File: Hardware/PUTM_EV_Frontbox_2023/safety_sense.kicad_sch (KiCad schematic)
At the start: 2 parts, among them U6 TLP291-4, U7 TLP291-4

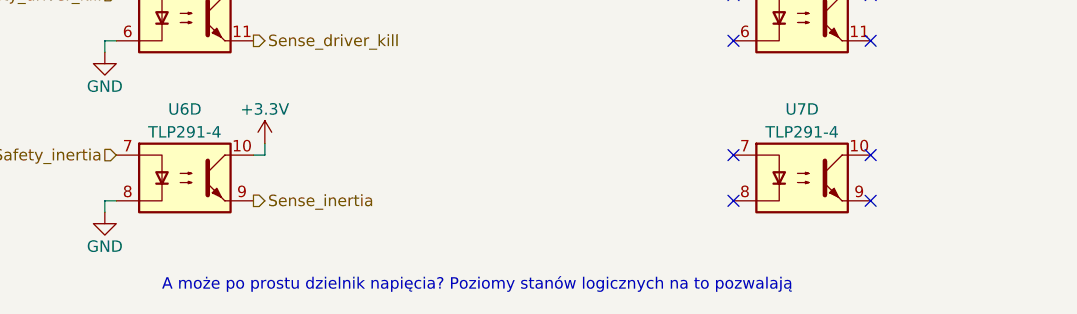
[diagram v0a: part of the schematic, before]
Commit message: Added power section, replaced SWPS
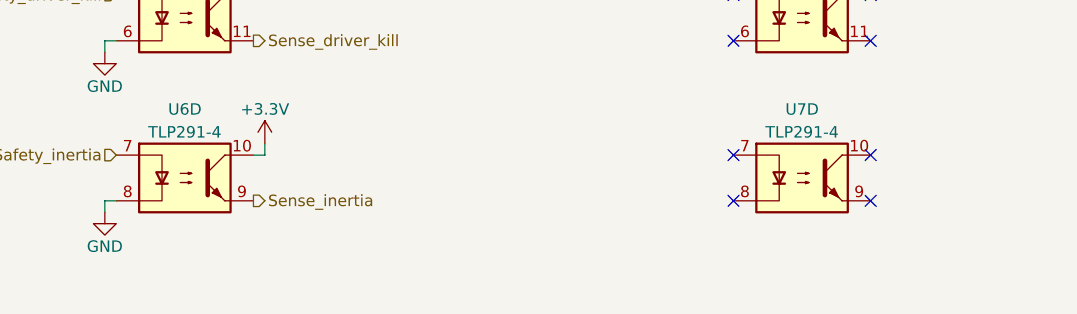
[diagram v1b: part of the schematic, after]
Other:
- note removed: "A może po prostu dzielnik napięcia? Poziomy stanów logicznych na to pozwalają"
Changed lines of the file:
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@@
     (stroke (width 0) (type default))
-  )
-  (text "A może po prostu dzielnik napięcia? Poziomy stanów logicznych na to pozwalają"
-    (at 110.49 142.24 0)
-    (effects (font (size 1.27 1.27)) (justify left bottom))
   )
   (hierarchical_label "Safety_right_kill" (shape input) (at 105.41 92.71 180) (fields_autoplaced)

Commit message: Schematic ready for review
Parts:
- removed unit 4 of U7
- added R11, R12, R13, R14, R15, R16: 5k, symbol Device:R_Small
- renumbered U6 to U10, U7 to U11
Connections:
- net Safety_BSPD: now also R15.1; no longer U11.1
- net Safety_driver_kill: now also R13.1; no longer U10.5
- net Safety_inertia: now also R14.1; no longer U10.7
- net Safety_left_kill: now also R11.1; no longer U10.1
- net Safety_overtravel: now also R16.1; no longer U11.3
- net Safety_right_kill: now also R12.1; no longer U10.3
- new net: R16.2, U11.3
- new net: R12.2, U10.3
- new net: R11.2, U10.1
- new net: R14.2, U10.7
- new net: R13.2, U10.5
- new net: R15.2, U11.1
- no-connect marks 8 -> 4
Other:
- note added: "The remaining optocoupler is used to translate laptimer states"
- moved on the sheet: U10B, U10C, U10D, U11B, U11C

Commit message: Fixed all issues
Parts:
- added R79, R80, R81, R82, R83, R84: 10k, symbol Device:R_Small
- R11, R12, R13, R14, R15, R16: value 5k -> 2k
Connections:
- net +3.3V: now also R79.1, R80.1, R81.1, R82.1, R83.1, R84.1; no longer U10.10, U10.12, U10.14, U10.16, U11.14, U11.16
- net GND: now also U10.11, U10.13, U10.15, U10.9, U11.13, U11.15
- net Sense_BSPD: now also U11.16, R83.2; no longer U11.15
- net Sense_driver_kill: now also U10.12, R81.2; no longer U10.11
- net Sense_inertia: now also U10.10, R82.2; no longer U10.9
- net Sense_left_kill: now also U10.16, R79.2; no longer U10.15
- net Sense_overtravel: now also U11.14, R84.2; no longer U11.13
- net Sense_right_kill: now also U10.14, R80.2; no longer U10.13
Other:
- moved on the sheet: R12, R13, R14, R16, U10B, U10C, U10D, U11B, U11C

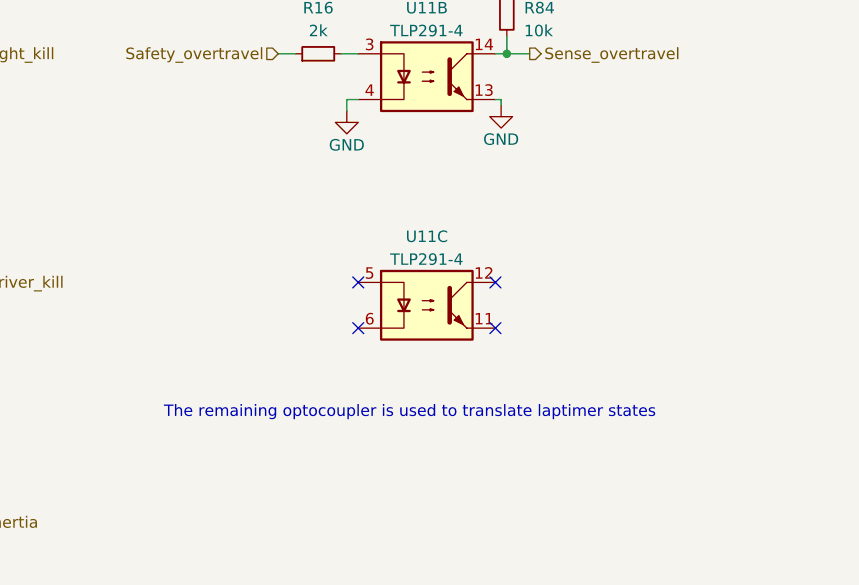
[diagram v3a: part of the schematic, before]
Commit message: Schematic modified, footprints assigned
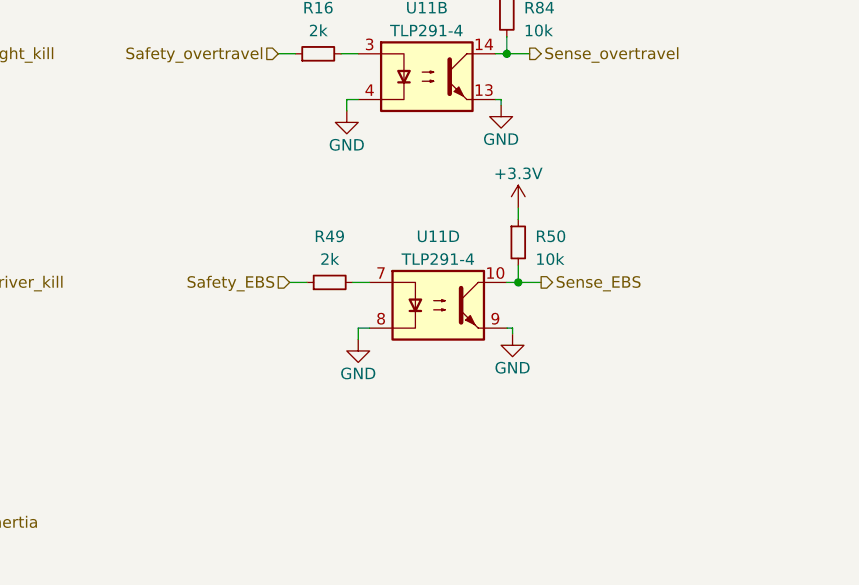
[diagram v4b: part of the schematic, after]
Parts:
- removed unit 3 of U11
- added R49: 2k, Resistor_SMD:R_0402_1005Metric, symbol Device:R_Small
- added R50: 10k, Resistor_SMD:R_0402_1005Metric, symbol Device:R_Small
- added unit 4 of U11
- R11, R12, R13, R14, R15, R16, R79, R80, R81, R82, R83, R84: footprint (none) -> Resistor_SMD:R_0402_1005Metric
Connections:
- net +3.3V: now also R50.1
- net GND: now also U11.8, U11.9
- new net: R49.2, U11.7
- new net Safety_EBS: R49.1
- new net Sense_EBS: R50.2, U11.10
- no-connect marks 4 -> 0
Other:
- note removed: "The remaining optocoupler is used to translate laptimer states"

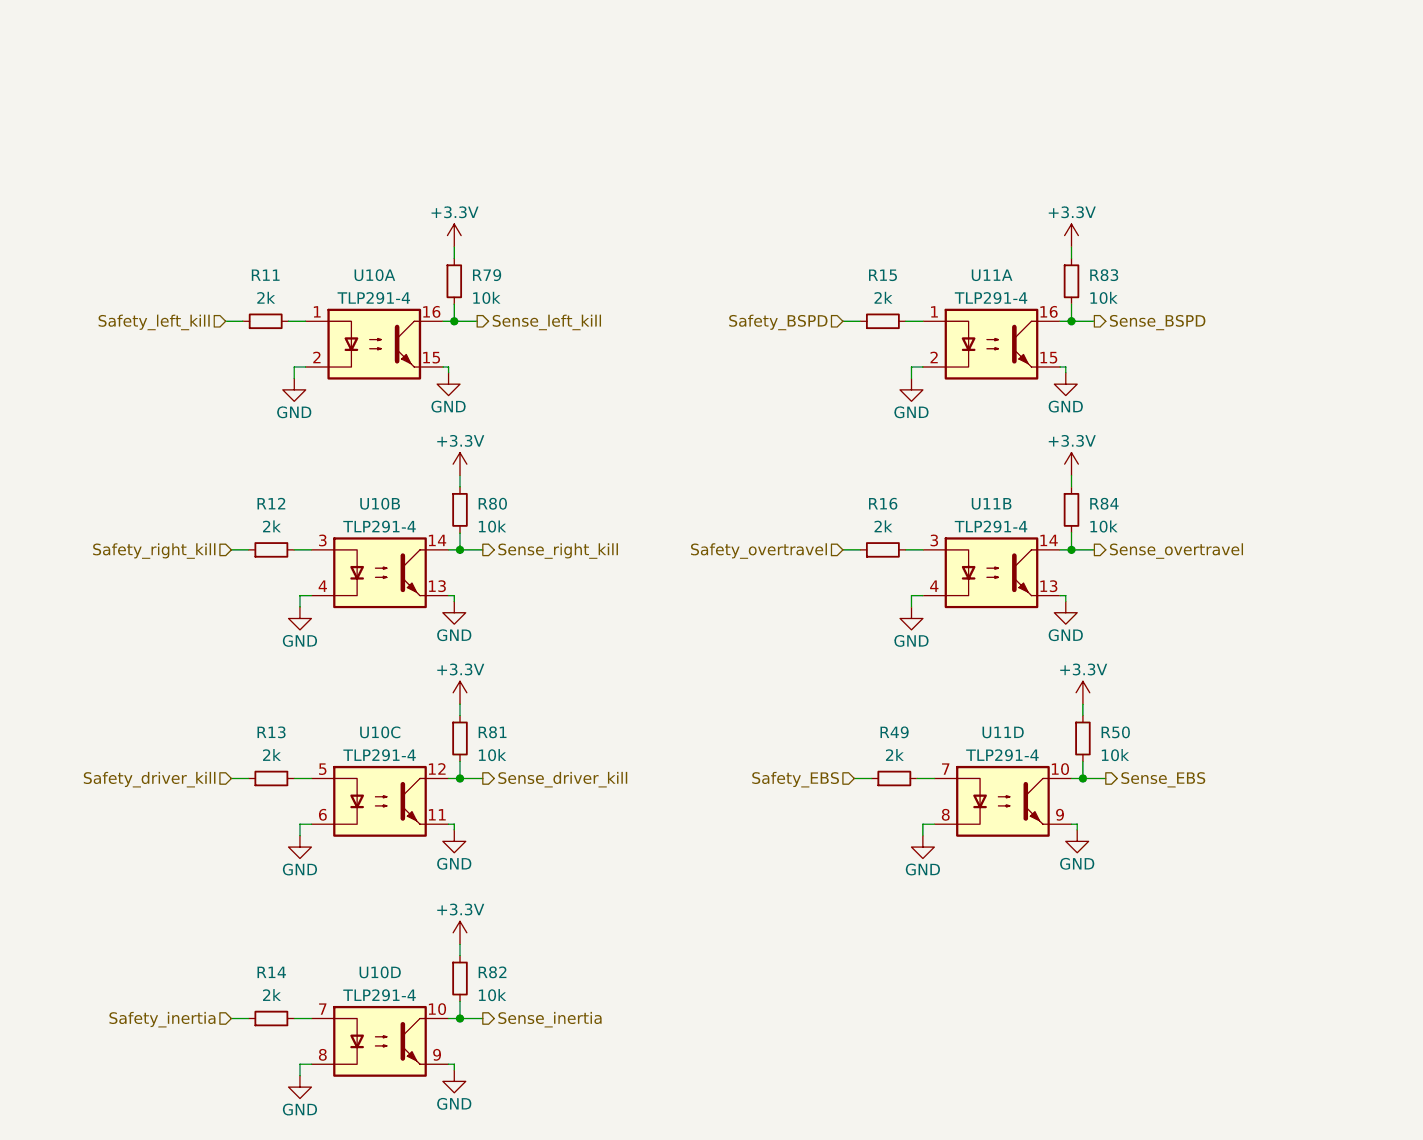
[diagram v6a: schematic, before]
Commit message: Changed board outline and layout to match ASB
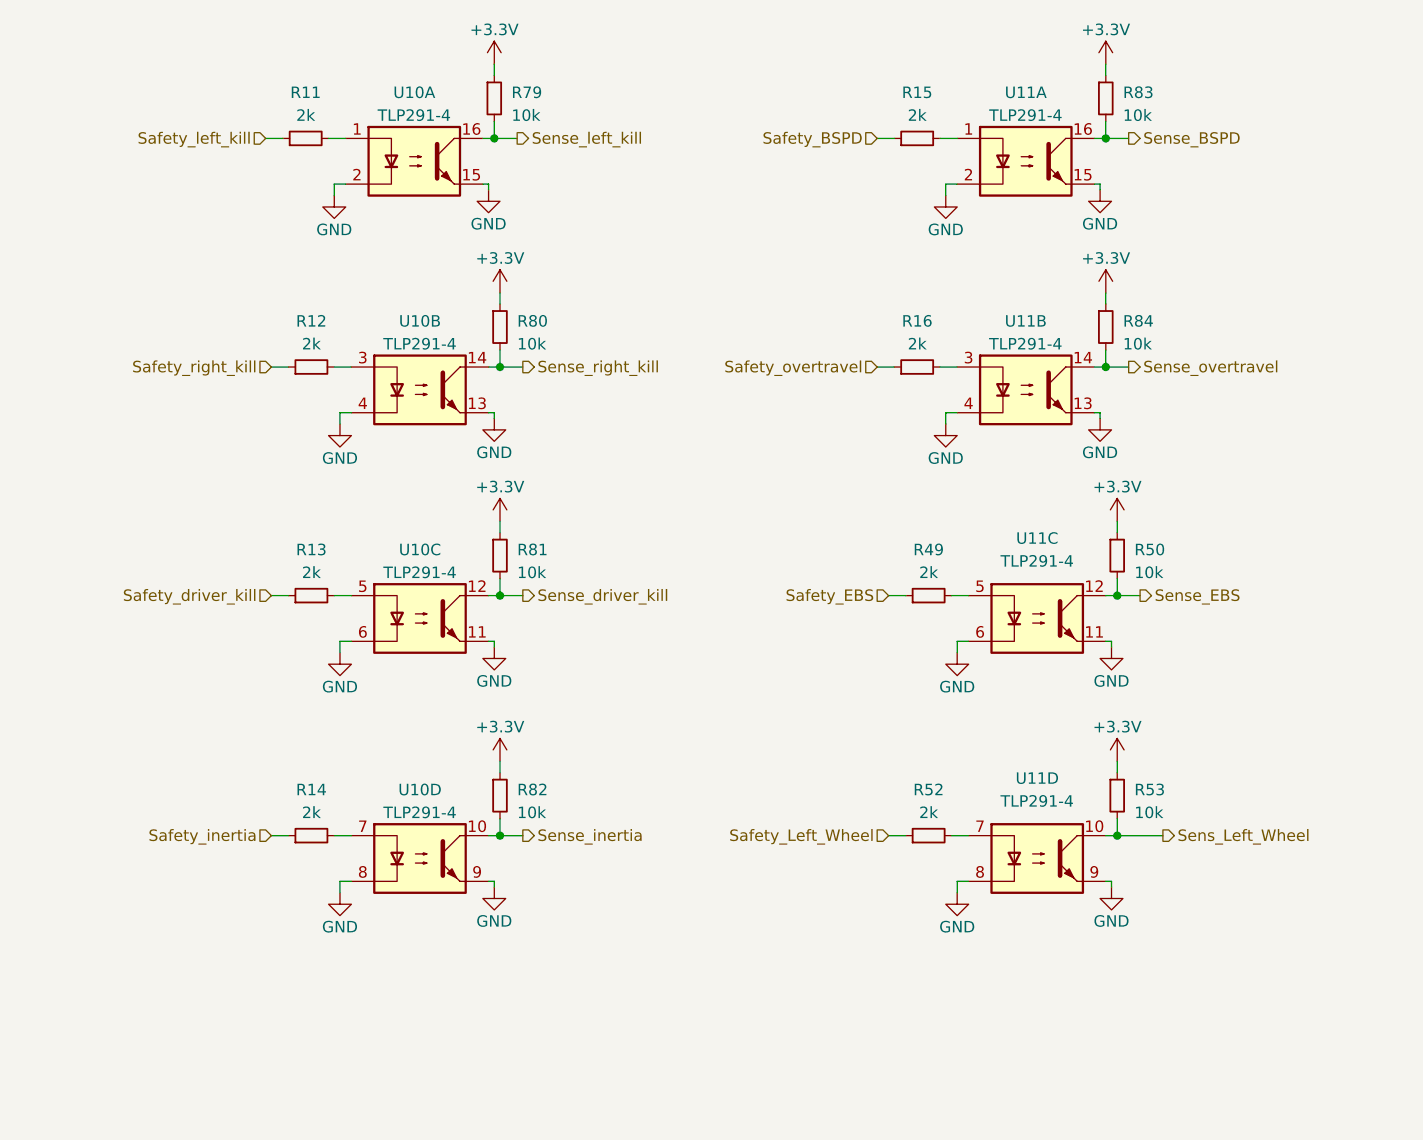
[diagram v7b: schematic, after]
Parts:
- added R52: 2k, Resistor_SMD:R_0402_1005Metric, symbol Device:R_Small
- added R53: 10k, Resistor_SMD:R_0402_1005Metric, symbol Device:R_Small
- added unit 4 of U11
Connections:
- net +3.3V: now also R53.1
- net GND: now also U11.11, U11.6, U11.8, U11.9; no longer U11.8, U11.9
- net Sense_EBS: now also U11.12; no longer U11.10
- net at R49.2: now also U11.5; no longer U11.7
- new net: R52.2, U11.7
- new net Safety_Left_Wheel: R52.1
- new net Sens_Left_Wheel: R53.2, U11.10
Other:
- moved on the sheet: R11, R12, R13, R14, R15, R16, R49, R50, R79, R80, R81, R82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

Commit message: Changed mcu pinout
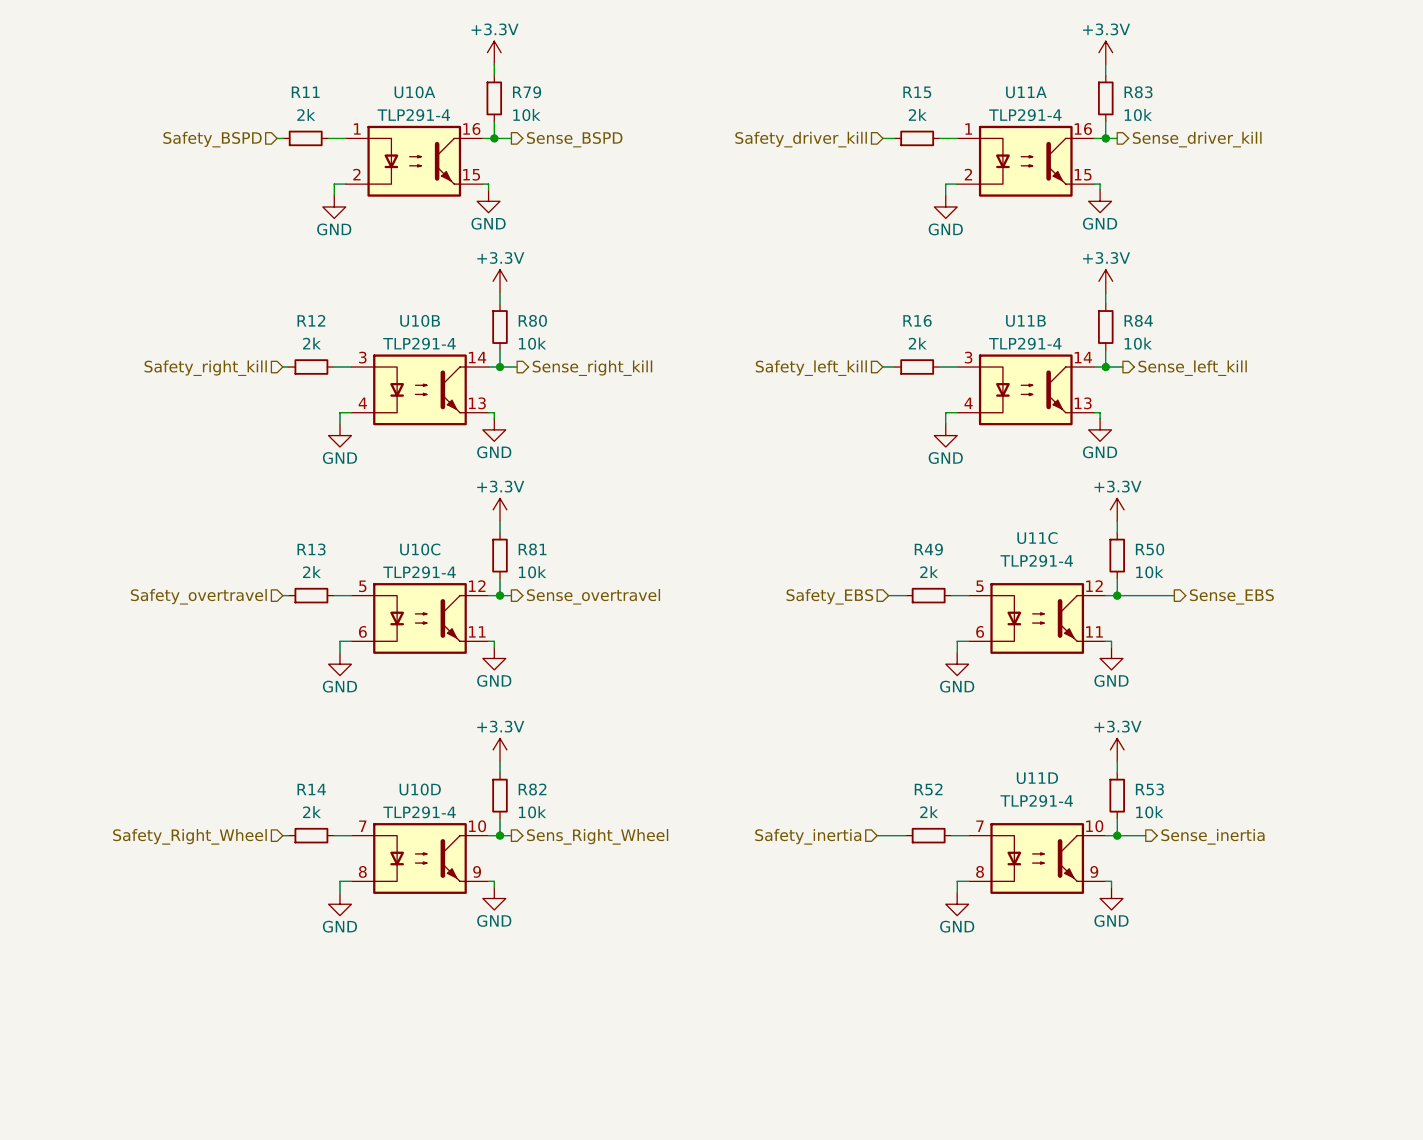
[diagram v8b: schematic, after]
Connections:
- net Safety_Left_Wheel is gone; now on net Safety_inertia: R52.1
- net Sens_Left_Wheel is gone; now on net Sense_inertia: R53.2, U11.10
- net Safety_BSPD: now also R11.1; no longer R15.1
- net Safety_driver_kill: now also R15.1; no longer R13.1
- net Safety_inertia: no longer R14.1
- net Safety_left_kill: now also R16.1; no longer R11.1
- net Safety_overtravel: now also R13.1; no longer R16.1
- net Sense_BSPD: now also R79.2, U10.16; no longer R83.2, U11.16
- net Sense_driver_kill: now also R83.2, U11.16; no longer R81.2, U10.12
- net Sense_inertia: no longer R82.2, U10.10
- net Sense_left_kill: now also R84.2, U11.14; no longer R79.2, U10.16
- net Sense_overtravel: now also R81.2, U10.12; no longer R84.2, U11.14
- new net Safety_Right_Wheel: R14.1
- new net Sens_Right_Wheel: R82.2, U10.10
